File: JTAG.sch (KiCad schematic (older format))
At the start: 27 parts, among them CN1 2x5_Way_1.27mm_Pitch_Header, CN5 CONN_RCPT_USB2.0_MINI_B_SMD_R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, U15 FT2232HL-REEL, X2 ABM3B-12.000MHZ

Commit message: JTAG pins have added
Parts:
- CN1: symbol OpenVent-rescue:Header_2x5-OpenVent -> OpenVent:Header_2x5
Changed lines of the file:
@@
 	10300 3350 9550 3350
 $Comp
-L OpenVent-rescue:Header_2x5-OpenVent CN?
+L OpenVent:Header_2x5 CN?
 U 1 1 603F320C
 P 9050 3200

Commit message: Header symbol has been replaced
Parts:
- removed CN1: 2x5_Way_1.27mm_Pitch_Header, symbol OpenVent:Header_2x5
- added CN?: 2x5_Way_1.27mm_Pitch_Header, symbol OpenVent:2x5_Way_1.27mm_Pitch_Header
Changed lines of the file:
@@
 Wire Wire Line
 	10300 3350 9550 3350
-$Comp
-L OpenVent:Header_2x5 CN?
-U 1 1 603F320C
-P 9050 3200
-AR Path="/603F320C" Ref="CN?"  Part="1"
-AR Path="/5F8F8987/603F320C" Ref="CN1"  Part="1"
-F 0 "CN1" H 9050 3275 50  0000 C CNN
-F 1 "2x5_Way_1.27mm_Pitch_Header" H 9050 3184 50  0000 C CNN
-F 2 "" H 9050 3200 50  0001 C CNN
-F 3 "http://www.cnctech.us/idcmatching2.pdf" H 9050 3200 50  0001 C CNN
-	1    9050 3200
-	1    0    0    -1
-$EndComp
 Text GLabel 10175 3750 2    50   Output ~ 0
 NRST
@@
 Wire Wire Line
 	7775 2700 7875 2700
+$Comp
+L OpenVent:2x5_Way_1.27mm_Pitch_Header CN?
+U 1 1 6053C246
+P 9050 3200
+F 0 "CN?" H 9050 3275 50  0000 C CNN
+F 1 "2x5_Way_1.27mm_Pitch_Header" H 9050 3184 50  0000 C CNN
+F 2 "" H 9050 3200 50  0001 C CNN
+F 3 "http://www.cnctech.us/idcmatching2.pdf" H 9050 3200 50  0001 C CNN
+	1    9050 3200
+	1    0    0    -1
+$EndComp
 $EndSCHEMATC

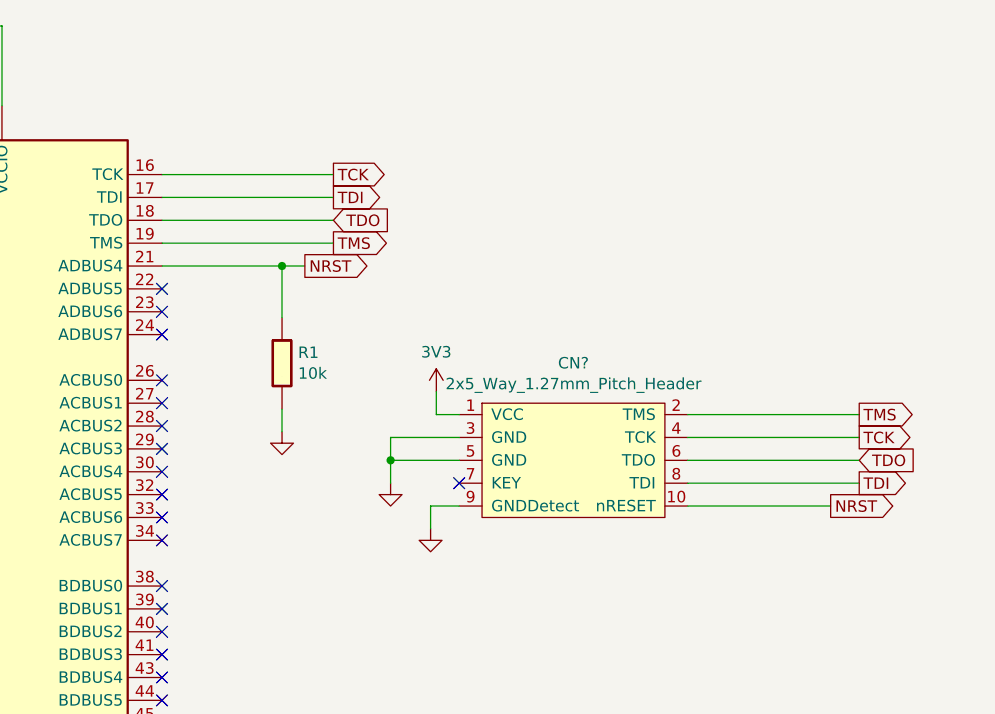
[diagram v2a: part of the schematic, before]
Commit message: JTAG header have been put on FTDI chip output
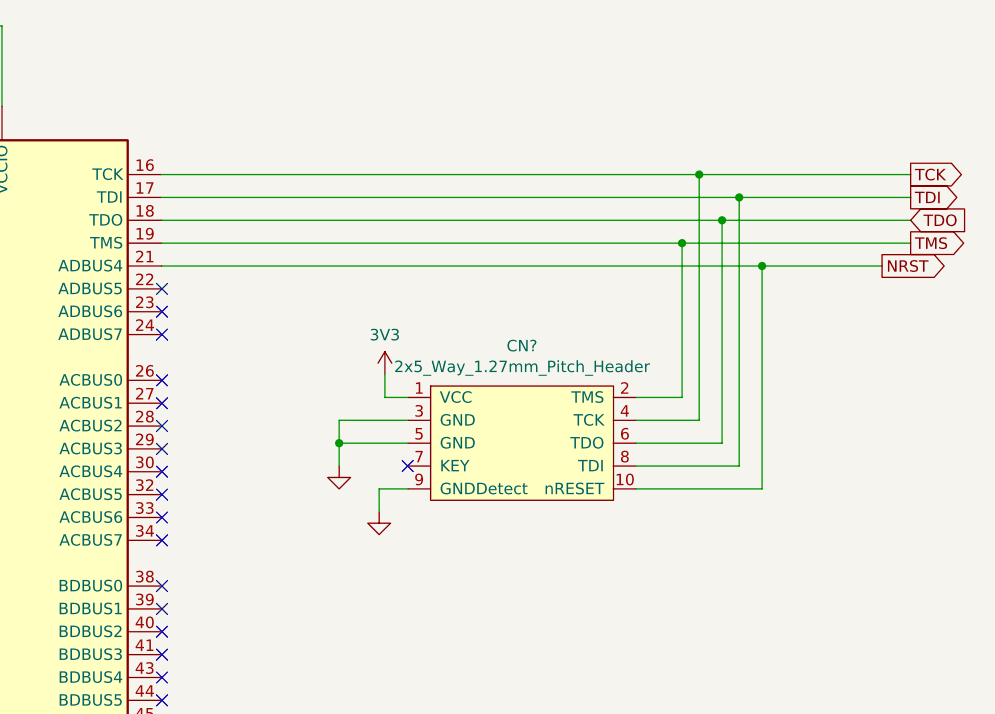
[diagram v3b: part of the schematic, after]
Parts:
- removed R1: 10k_0603_Chip_Resistor,_1%,_0.1W, symbol OpenVent:10k_0603_Chip_Resistor,_1%,_0.1W
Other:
- moved on the sheet: CN?
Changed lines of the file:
@@
 Wire Wire Line
 	4200 5100 4200 5150
-Text GLabel 8000 2300 2    50   Output ~ 0
+Text GLabel 10525 2300 2    50   Output ~ 0
 TCK
-Text GLabel 8000 2400 2    50   Output ~ 0
+Text GLabel 10525 2400 2    50   Output ~ 0
 TDI
-Text GLabel 8000 2500 2    50   Input ~ 0
+Text GLabel 10525 2500 2    50   Input ~ 0
 TDO
-Text GLabel 8000 2600 2    50   Output ~ 0
+Text GLabel 10525 2600 2    50   Output ~ 0
 TMS
-Wire Wire Line
-	7250 2300 8000 2300
-Wire Wire Line
-	8000 2400 7250 2400
-Wire Wire Line
-	7250 2500 8000 2500
-Wire Wire Line
-	8000 2600 7250 2600
 NoConn ~ 1400 3500
 NoConn ~ 3150 3850
@@
 L OpenVent:GND #PWR02
 U 1 1 603ABA41
-P 8250 3650
-F 0 "#PWR02" H 8250 3400 50  0001 C CNN
-F 1 "GND" H 8250 3500 50  0001 C CNN
-F 2 "" H 8250 3650 50  0001 C CNN
-F 3 "" H 8250 3650 50  0001 C CNN
-	1    8250 3650
+P 8025 3575
+F 0 "#PWR02" H 8025 3325 50  0001 C CNN
+F 1 "GND" H 8025 3425 50  0001 C CNN
+F 2 "" H 8025 3575 50  0001 C CNN
+F 3 "" H 8025 3575 50  0001 C CNN
+	1    8025 3575
 	1    0    0    -1
 $EndComp
 Wire Wire Line
-	8550 3550 8250 3550
+	8325 3475 8025 3475
 Wire Wire Line
-	8250 3550 8250 3650
+	8025 3475 8025 3575
 Wire Wire Line
-	8550 3450 8250 3450
+	8325 3375 8025 3375
 Wire Wire Line
-	8250 3450 8250 3550
-Connection ~ 8250 3550
+	8025 3375 8025 3475
+Connection ~ 8025 3475
 $Comp
 L OpenVent:3V3 #PWR04
 U 1 1 603BA4C8
-P 8450 3250
-F 0 "#PWR04" H 8450 3100 50  0001 C CNN
-F 1 "3V3" H 8450 3423 50  0000 C CNN
-F 2 "" H 8450 3250 50  0001 C CNN
-F 3 "" H 8450 3250 50  0001 C CNN
-	1    8450 3250
+P 8225 3175
+F 0 "#PWR04" H 8225 3025 50  0001 C CNN
+F 1 "3V3" H 8225 3348 50  0000 C CNN
+F 2 "" H 8225 3175 50  0001 C CNN
+F 3 "" H 8225 3175 50  0001 C CNN
+	1    8225 3175
 	1    0    0    -1
 $EndComp
 Wire Wire Line
-	8450 3250 8450 3350
+	8225 3175 8225 3275
 Wire Wire Line
-	8450 3350 8550 3350
-Text GLabel 10300 3450 2    50   Output ~ 0
-TCK
+	8225 3275 8325 3275
 Wire Wire Line
-	9550 3450 10300 3450
-Text GLabel 10300 3650 2    50   Output ~ 0
-TDI
-Text GLabel 10300 3550 2    50   Input ~ 0
-TDO
-Text GLabel 10300 3350 2    50   Output ~ 0
-TMS
+	9325 3375 9600 3375
 Wire Wire Line
-	10300 3650 9550 3650
-Wire Wire Line
-	9550 3550 10300 3550
-Wire Wire Line
-	10300 3350 9550 3350
-Text GLabel 10175 3750 2    50   Output ~ 0
-NRST
-Wire Wire Line
-	9550 3750 10175 3750
+	9325 3475 9700 3475
 $Comp
 L OpenVent:GND #PWR03
 U 1 1 6041AEF9
-P 8425 3850
-F 0 "#PWR03" H 8425 3600 50  0001 C CNN
-F 1 "GND" H 8425 3700 50  0001 C CNN
-F 2 "" H 8425 3850 50  0001 C CNN
-F 3 "" H 8425 3850 50  0001 C CNN
-	1    8425 3850
+P 8200 3775
+F 0 "#PWR03" H 8200 3525 50  0001 C CNN
+F 1 "GND" H 8200 3625 50  0001 C CNN
+F 2 "" H 8200 3775 50  0001 C CNN
+F 3 "" H 8200 3775 50  0001 C CNN
+	1    8200 3775
 	1    0    0    -1
 $EndComp
 Wire Wire Line
-	8425 3750 8425 3850
+	8200 3675 8200 3775
 Wire Wire Line
-	8425 3750 8550 3750
-NoConn ~ 8550 3650
-Text GLabel 7875 2700 2    50   Output ~ 0
+	8200 3675 8325 3675
+NoConn ~ 8325 3575
+Text GLabel 10400 2700 2    50   Output ~ 0
 NRST
 $Comp
-L OpenVent:10k_0603_Chip_Resistor,_1%,_0.1W R1
-U 1 1 6053B2C9
-P 7875 3025
-F 0 "R1" V 7929 2995 50  0000 L CNN
-F 1 "10k_0603_Chip_Resistor,_1%,_0.1W" H 7875 3025 50  0001 C CNN
-F 2 "" H 7875 3025 50  0001 C CNN
-F 3 "" H 7875 3025 50  0001 C CNN
-F 4 "10k" V 8020 2995 50  0000 L CNN "Val"
-F 5 "1%" H 7875 3025 50  0001 C CNN "Tolerance"
-F 6 "0.1W" H 7875 3025 50  0001 C CNN "Watt"
-	1    7875 3025
-	0    1    1    0
-$EndComp
-$Comp
-L OpenVent:GND #PWR01
-U 1 1 6053CC72
-P 7775 3425
-F 0 "#PWR01" H 7775 3175 50  0001 C CNN
-F 1 "GND" H 7775 3275 50  0001 C CNN
-F 2 "" H 7775 3425 50  0001 C CNN
-F 3 "" H 7775 3425 50  0001 C CNN
-	1    7775 3425
+L OpenVent:2x5_Way_1.27mm_Pitch_Header CN?
+U 1 1 6053C246
+P 8825 3125
+F 0 "CN?" H 8825 3200 50  0000 C CNN
+F 1 "2x5_Way_1.27mm_Pitch_Header" H 8825 3109 50  0000 C CNN
+F 2 "" H 8825 3125 50  0001 C CNN
+F 3 "http://www.cnctech.us/idcmatching2.pdf" H 8825 3125 50  0001 C CNN
+	1    8825 3125
 	1    0    0    -1
 $EndComp
 Wire Wire Line
-	7775 3325 7775 3425
+	7250 2300 9600 2300
 Wire Wire Line
-	7250 2700 7775 2700
+	7250 2400 9775 2400
 Wire Wire Line
-	7775 2925 7775 2700
-Connection ~ 7775 2700
+	7250 2500 9700 2500
 Wire Wire Line
-	7775 2700 7875 2700
-$Comp
-L OpenVent:2x5_Way_1.27mm_Pitch_Header CN?
-U 1 1 6053C246
-P 9050 3200
-F 0 "CN?" H 9050 3275 50  0000 C CNN
-F 1 "2x5_Way_1.27mm_Pitch_Header" H 9050 3184 50  0000 C CNN
-F 2 "" H 9050 3200 50  0001 C CNN
-F 3 "http://www.cnctech.us/idcmatching2.pdf" H 9050 3200 50  0001 C CNN
-	1    9050 3200
-	1    0    0    -1
-$EndComp
+	7250 2600 9525 2600
+Wire Wire Line
+	9525 3275 9525 2600
+Wire Wire Line
+	9525 3275 9325 3275
+Connection ~ 9525 2600
+Wire Wire Line
+	9525 2600 10525 2600
+Wire Wire Line
+	9600 3375 9600 2300
+Connection ~ 9600 2300
+Wire Wire Line
+	9600 2300 10525 2300
+Wire Wire Line
+	9700 3475 9700 2500
+Connection ~ 9700 2500
+Wire Wire Line
+	9700 2500 10525 2500
+Wire Wire Line
+	9775 3575 9775 2400
+Wire Wire Line
+	9775 3575 9325 3575
+Connection ~ 9775 2400
+Wire Wire Line
+	9775 2400 10525 2400
+Wire Wire Line
+	9875 3675 9875 2700
+Wire Wire Line
+	9325 3675 9875 3675
+Connection ~ 9875 2700
+Wire Wire Line
+	9875 2700 10400 2700
+Wire Wire Line
+	7250 2700 9875 2700
 $EndSCHEMATC

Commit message: PWM and SPI_FPGA_CS pins swapped on MCU
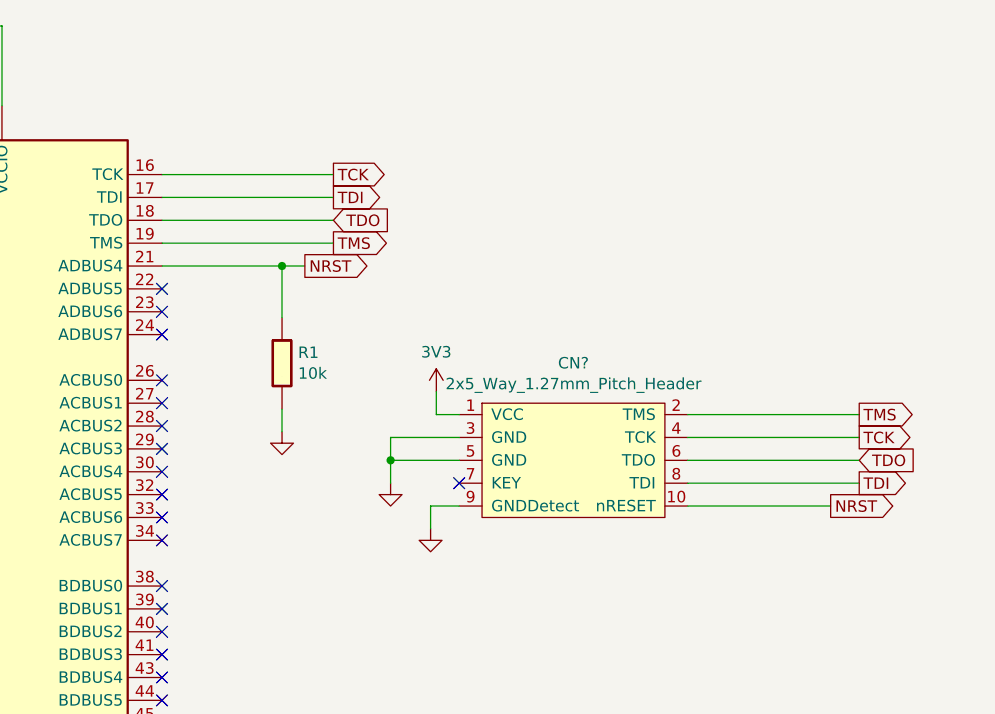
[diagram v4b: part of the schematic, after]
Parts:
- added R1: 10k_0603_Chip_Resistor,_1%,_0.1W, symbol OpenVent:10k_0603_Chip_Resistor,_1%,_0.1W
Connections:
- net GND: now also R1.2
- net NRST: now also R1.1
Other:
- moved on the sheet: CN?
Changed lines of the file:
@@
 Wire Wire Line
 	4200 5100 4200 5150
-Text GLabel 10525 2300 2    50   Output ~ 0
+Text GLabel 8000 2300 2    50   Output ~ 0
 TCK
-Text GLabel 10525 2400 2    50   Output ~ 0
+Text GLabel 8000 2400 2    50   Output ~ 0
 TDI
-Text GLabel 10525 2500 2    50   Input ~ 0
+Text GLabel 8000 2500 2    50   Input ~ 0
 TDO
-Text GLabel 10525 2600 2    50   Output ~ 0
+Text GLabel 8000 2600 2    50   Output ~ 0
 TMS
+Wire Wire Line
+	7250 2300 8000 2300
+Wire Wire Line
+	8000 2400 7250 2400
+Wire Wire Line
+	7250 2500 8000 2500
+Wire Wire Line
+	8000 2600 7250 2600
 NoConn ~ 1400 3500
 NoConn ~ 3150 3850
@@
 L OpenVent:GND #PWR02
 U 1 1 603ABA41
-P 8025 3575
-F 0 "#PWR02" H 8025 3325 50  0001 C CNN
-F 1 "GND" H 8025 3425 50  0001 C CNN
-F 2 "" H 8025 3575 50  0001 C CNN
-F 3 "" H 8025 3575 50  0001 C CNN
-	1    8025 3575
+P 8250 3650
+F 0 "#PWR02" H 8250 3400 50  0001 C CNN
+F 1 "GND" H 8250 3500 50  0001 C CNN
+F 2 "" H 8250 3650 50  0001 C CNN
+F 3 "" H 8250 3650 50  0001 C CNN
+	1    8250 3650
 	1    0    0    -1
 $EndComp
 Wire Wire Line
-	8325 3475 8025 3475
+	8550 3550 8250 3550
 Wire Wire Line
-	8025 3475 8025 3575
+	8250 3550 8250 3650
 Wire Wire Line
-	8325 3375 8025 3375
+	8550 3450 8250 3450
 Wire Wire Line
-	8025 3375 8025 3475
-Connection ~ 8025 3475
+	8250 3450 8250 3550
+Connection ~ 8250 3550
 $Comp
 L OpenVent:3V3 #PWR04
 U 1 1 603BA4C8
-P 8225 3175
-F 0 "#PWR04" H 8225 3025 50  0001 C CNN
-F 1 "3V3" H 8225 3348 50  0000 C CNN
-F 2 "" H 8225 3175 50  0001 C CNN
-F 3 "" H 8225 3175 50  0001 C CNN
-	1    8225 3175
+P 8450 3250
+F 0 "#PWR04" H 8450 3100 50  0001 C CNN
+F 1 "3V3" H 8450 3423 50  0000 C CNN
+F 2 "" H 8450 3250 50  0001 C CNN
+F 3 "" H 8450 3250 50  0001 C CNN
+	1    8450 3250
 	1    0    0    -1
 $EndComp
 Wire Wire Line
-	8225 3175 8225 3275
+	8450 3250 8450 3350
 Wire Wire Line
-	8225 3275 8325 3275
+	8450 3350 8550 3350
+Text GLabel 10300 3450 2    50   Output ~ 0
+TCK
 Wire Wire Line
-	9325 3375 9600 3375
+	9550 3450 10300 3450
+Text GLabel 10300 3650 2    50   Output ~ 0
+TDI
+Text GLabel 10300 3550 2    50   Input ~ 0
+TDO
+Text GLabel 10300 3350 2    50   Output ~ 0
+TMS
 Wire Wire Line
-	9325 3475 9700 3475
+	10300 3650 9550 3650
+Wire Wire Line
+	9550 3550 10300 3550
+Wire Wire Line
+	10300 3350 9550 3350
+Text GLabel 10175 3750 2    50   Output ~ 0
+NRST
+Wire Wire Line
+	9550 3750 10175 3750
 $Comp
 L OpenVent:GND #PWR03
 U 1 1 6041AEF9
-P 8200 3775
-F 0 "#PWR03" H 8200 3525 50  0001 C CNN
-F 1 "GND" H 8200 3625 50  0001 C CNN
-F 2 "" H 8200 3775 50  0001 C CNN
-F 3 "" H 8200 3775 50  0001 C CNN
-	1    8200 3775
+P 8425 3850
+F 0 "#PWR03" H 8425 3600 50  0001 C CNN
+F 1 "GND" H 8425 3700 50  0001 C CNN
+F 2 "" H 8425 3850 50  0001 C CNN
+F 3 "" H 8425 3850 50  0001 C CNN
+	1    8425 3850
 	1    0    0    -1
 $EndComp
 Wire Wire Line
-	8200 3675 8200 3775
+	8425 3750 8425 3850
 Wire Wire Line
-	8200 3675 8325 3675
-NoConn ~ 8325 3575
-Text GLabel 10400 2700 2    50   Output ~ 0
+	8425 3750 8550 3750
+NoConn ~ 8550 3650
+Text GLabel 7875 2700 2    50   Output ~ 0
 NRST
+$Comp
+L OpenVent:10k_0603_Chip_Resistor,_1%,_0.1W R1
+U 1 1 6053B2C9
+P 7875 3025
+F 0 "R1" V 7929 2995 50  0000 L CNN
+F 1 "10k_0603_Chip_Resistor,_1%,_0.1W" H 7875 3025 50  0001 C CNN
+F 2 "" H 7875 3025 50  0001 C CNN
+F 3 "" H 7875 3025 50  0001 C CNN
+F 4 "10k" V 8020 2995 50  0000 L CNN "Val"
+F 5 "1%" H 7875 3025 50  0001 C CNN "Tolerance"
+F 6 "0.1W" H 7875 3025 50  0001 C CNN "Watt"
+	1    7875 3025
+	0    1    1    0
+$EndComp
+$Comp
+L OpenVent:GND #PWR01
+U 1 1 6053CC72
+P 7775 3425
+F 0 "#PWR01" H 7775 3175 50  0001 C CNN
+F 1 "GND" H 7775 3275 50  0001 C CNN
+F 2 "" H 7775 3425 50  0001 C CNN
+F 3 "" H 7775 3425 50  0001 C CNN
+	1    7775 3425
+	1    0    0    -1
+$EndComp
+Wire Wire Line
+	7775 3325 7775 3425
+Wire Wire Line
+	7250 2700 7775 2700
+Wire Wire Line
+	7775 2925 7775 2700
+Connection ~ 7775 2700
+Wire Wire Line
+	7775 2700 7875 2700
 $Comp
 L OpenVent:2x5_Way_1.27mm_Pitch_Header CN?
 U 1 1 6053C246
-P 8825 3125
-F 0 "CN?" H 8825 3200 50  0000 C CNN
-F 1 "2x5_Way_1.27mm_Pitch_Header" H 8825 3109 50  0000 C CNN
-F 2 "" H 8825 3125 50  0001 C CNN
-F 3 "http://www.cnctech.us/idcmatching2.pdf" H 8825 3125 50  0001 C CNN
-	1    8825 3125
+P 9050 3200
+F 0 "CN?" H 9050 3275 50  0000 C CNN
+F 1 "2x5_Way_1.27mm_Pitch_Header" H 9050 3184 50  0000 C CNN
+F 2 "" H 9050 3200 50  0001 C CNN
+F 3 "http://www.cnctech.us/idcmatching2.pdf" H 9050 3200 50  0001 C CNN
+	1    9050 3200
 	1    0    0    -1
 $EndComp
-Wire Wire Line
-	7250 2300 9600 2300
-Wire Wire Line
-	7250 2400 9775 2400
-Wire Wire Line
-	7250 2500 9700 2500
-Wire Wire Line
-	7250 2600 9525 2600
-Wire Wire Line
-	9525 3275 9525 2600
-Wire Wire Line
-	9525 3275 9325 3275
-Connection ~ 9525 2600
-Wire Wire Line
-	9525 2600 10525 2600
-Wire Wire Line
-	9600 3375 9600 2300
-Connection ~ 9600 2300
-Wire Wire Line
-	9600 2300 10525 2300
-Wire Wire Line
-	9700 3475 9700 2500
-Connection ~ 9700 2500
-Wire Wire Line
-	9700 2500 10525 2500
-Wire Wire Line
-	9775 3575 9775 2400
-Wire Wire Line
-	9775 3575 9325 3575
-Connection ~ 9775 2400
-Wire Wire Line
-	9775 2400 10525 2400
-Wire Wire Line
-	9875 3675 9875 2700
-Wire Wire Line
-	9325 3675 9875 3675
-Connection ~ 9875 2700
-Wire Wire Line
-	9875 2700 10400 2700
-Wire Wire Line
-	7250 2700 9875 2700
 $EndSCHEMATC

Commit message: Update JTAG.sch
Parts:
- added D?: LED_GREEN_0603_SMD, symbol OpenVent:LED_GREEN_0603_SMD
- added D?: LED_Red_0603_SMD, symbol OpenVent:LED_Red_0603_SMD
- added J?: Reset_Switch, symbol Device:CircuitBreaker_1P
- added R? (x4): 12k_0603_Chip_Resistor,_1%,_0.1W, Resistor_SMD:R_0603_1608Metric, symbol OpenVent:12k_0603_Chip_Resistor,_1%,_0.1W
- added R?: R_0603_200_0.1W_1%, Resistor_SMD:R_0603_1608Metric, symbol OpenVent:R_0603_200_0.1W_1%
- added R? (x2): 1K_0603_Chip_Resistor,_1%,_0.1W, symbol OpenVent:1K_0603_Chip_Resistor,_1%,_0.1W
- added R?: R_0603_49k9_0.1W_1%, symbol OpenVent:R_0603_49k9_0.1W_1%
- added U?: GW1N-9LQ100, symbol OpenVent:GW1N-9LQ100
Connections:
- net +3V3: now also R?.1, R?.1, R?.1, R?.2
- net GND: now also D?.2 (CATHODE), R?.1, R?.1, R?.1, R?.2
- new net: J?.1, R?.1
- new net: D?.1 (ANODE), R?.2
- new net: R?.2, U?.3 (IOL5A/JTAGSEL_N/LPLL_T_in)
- new net CONFIG_N: J?.2, R?.2
- new net DONE: D?.1 (ANODE), D?.2 (CATHODE), R?.2
- new net READY: R?.1
- new net TCK_F: R?.2, U?.9 (IOL11B/TCK)
- new net TDI_F: U?.11 (IOL12B/TDI)
- new net TDO_F: U?.12 (IOL13A/TDO)
- new net TMS_F: U?.8 (IOL11A/TMS)
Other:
- note added: "FPGA JTAG\n"
- moved on the sheet: C41, C42, C43, C44, C45, C46, C47, C48, C49, C50, C51, C52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

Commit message: Update JTAG.sch
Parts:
- U?: symbol OpenVent:GW1N-9LQ100 -> OpenVent-rescue:GW1N-9LQ100-OpenVent
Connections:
- net CONFIG_N: now also U?.14 (RECONFIG_N/IOL13B)
- net DONE: now also U?.15 (DONE/IOL14A)
- net READY: now also U?.16 (READY/IOL14B)
- net at R?.2: now also U?.100 (MODE0)
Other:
- moved on the sheet: U?B
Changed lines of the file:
@@
 	9500 4500 9500 5000
 $Comp
-L OpenVent:GW1N-9LQ100 U?
+L OpenVent-rescue:GW1N-9LQ100-OpenVent U?
 U 2 1 6073BAD7
 P 8650 4900
 AR Path="/5FBE8499/6073BAD7" Ref="U?"  Part="2"
 AR Path="/5F8F8987/6073BAD7" Ref="U?"  Part="2"
+AR Path="/6073BAD7" Ref="U?"  Part="2"
 F 0 "U?" H 8675 5148 50  0000 C CNN
 F 1 "GW1N-9LQ100" H 8675 5057 50  0000 C CNN
